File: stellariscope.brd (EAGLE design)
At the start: 60.5 x 60.5 mm, 29 parts, among them U1 74238, U2 74238, U3 TLC5947PWP, U4 TLC59213, U5 741G79DCT, U6 74AHC1G126DBV, U7 74AHC1G126DBV, U8 74AHC1G32DBV, U9 74AHC1G32DBV

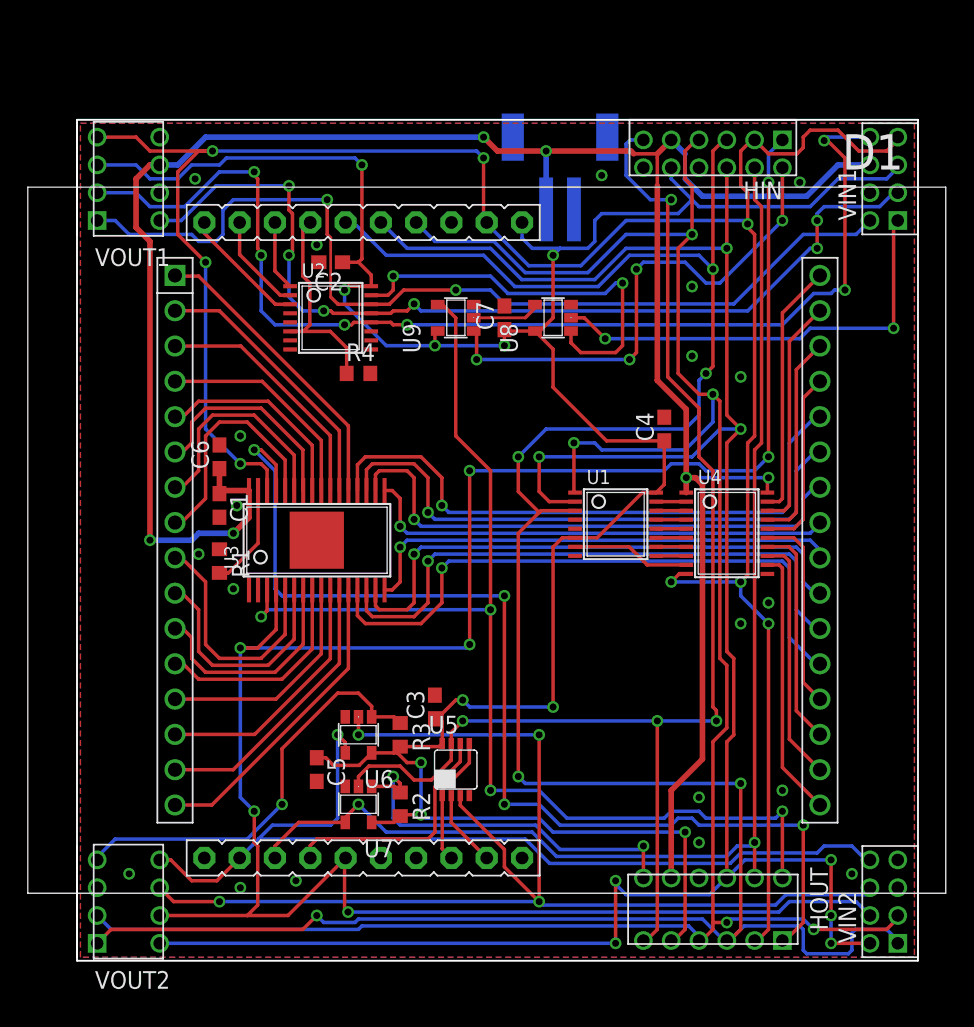
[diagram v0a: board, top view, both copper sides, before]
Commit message: This update fixes the issues with the board counting logic in the first edition. It also adds a driver to the XLAT line in order to prevent fanout problems in large array. This version has not been built and is unlikely to be built.
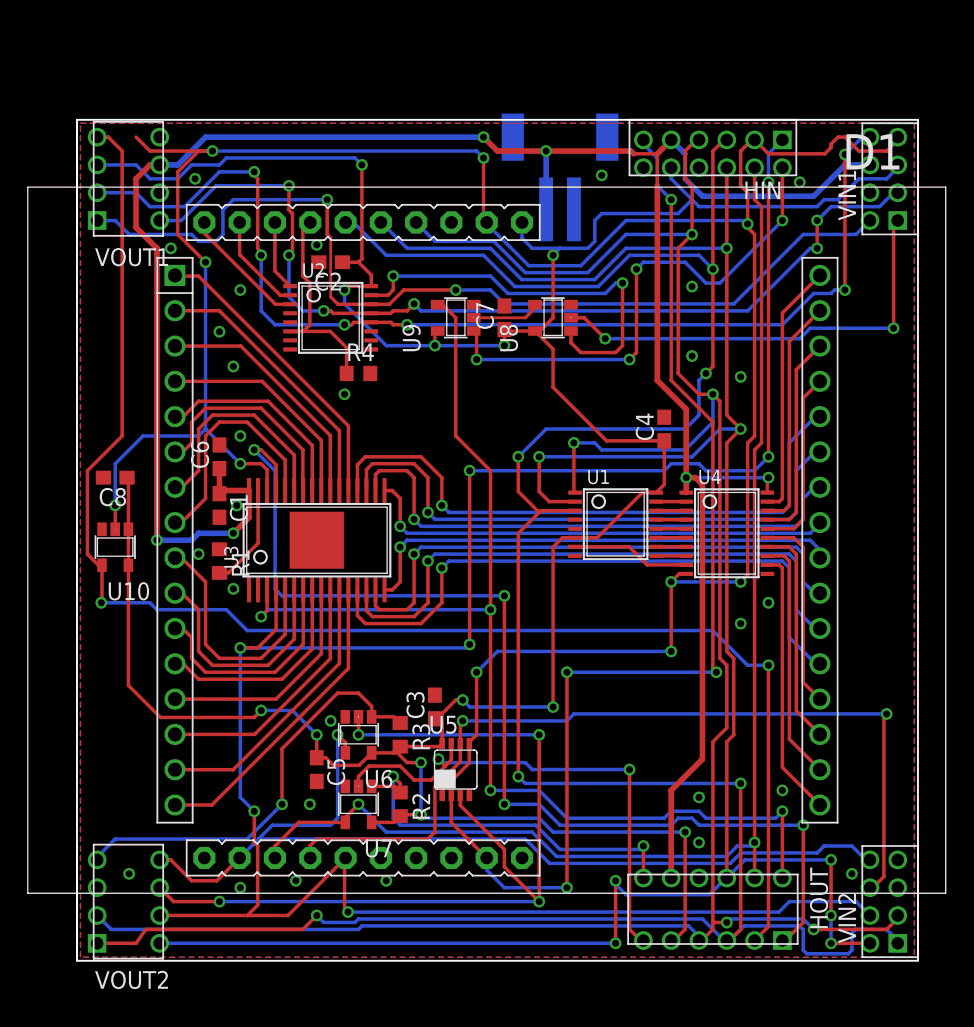
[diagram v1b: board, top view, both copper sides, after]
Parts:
- added C8: 100n, resistor:C0603
- added U10: 74AHC1G126DBV, 74xx-little-us:SOT23-5
- C1, C2, C3, C4, C5, C7: value (none) -> 100n
- C6: value (none) -> 1u
- R1: value (none) -> 2K7
- R2, R3, R4: value (none) -> 10K
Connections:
- net +3V3: now also C8.1, U10.1, U10.5
- net GND: now also C8.2, U10.3
- net HCNT_OUT: no longer HIN.11
- net N$28: now also HOUT.3, U10.4, VOUT1.7; no longer LAUNCHPAD.P2.7, U5.1, U5.5
- net N$37: now also HIN.11
- net N$38: now also VIN2.6
- net VCNT_OUT: no longer VIN2.6
- net XLAT: now also U10.2, U5.1, U5.5; no longer HOUT.3, VOUT1.7
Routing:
- net N$28: track 9.32 -> 106.4 mm, vias 0 -> 2
- net N$37: track 5.54 -> 79.4 mm, vias 0 -> 4
- net HCNT_OUT: track 93.1 -> 37.5 mm, vias 4 -> 2
- net N$38: track 17.4 -> 62.9 mm, vias 0 -> 2
- net +3V3: track 190.7 -> 222.7 mm, vias 10 -> 12
- net VCNT_OUT: track 88.5 -> 64.0 mm
- net XLAT: track 164.0 -> 175.1 mm, vias 8 -> 10
- net N$27: track 81.4 -> 78.9 mm

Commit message: -- Rotated Launchpad footprint to align with LED array -- Swapped vertical connectors to improve routing post-rotation -- Switched power on TLC5947 to 3V3, in order to accomodate logic levels -- Relocated power and horizontal connectors to midline (more or less) -- Added mounting holes
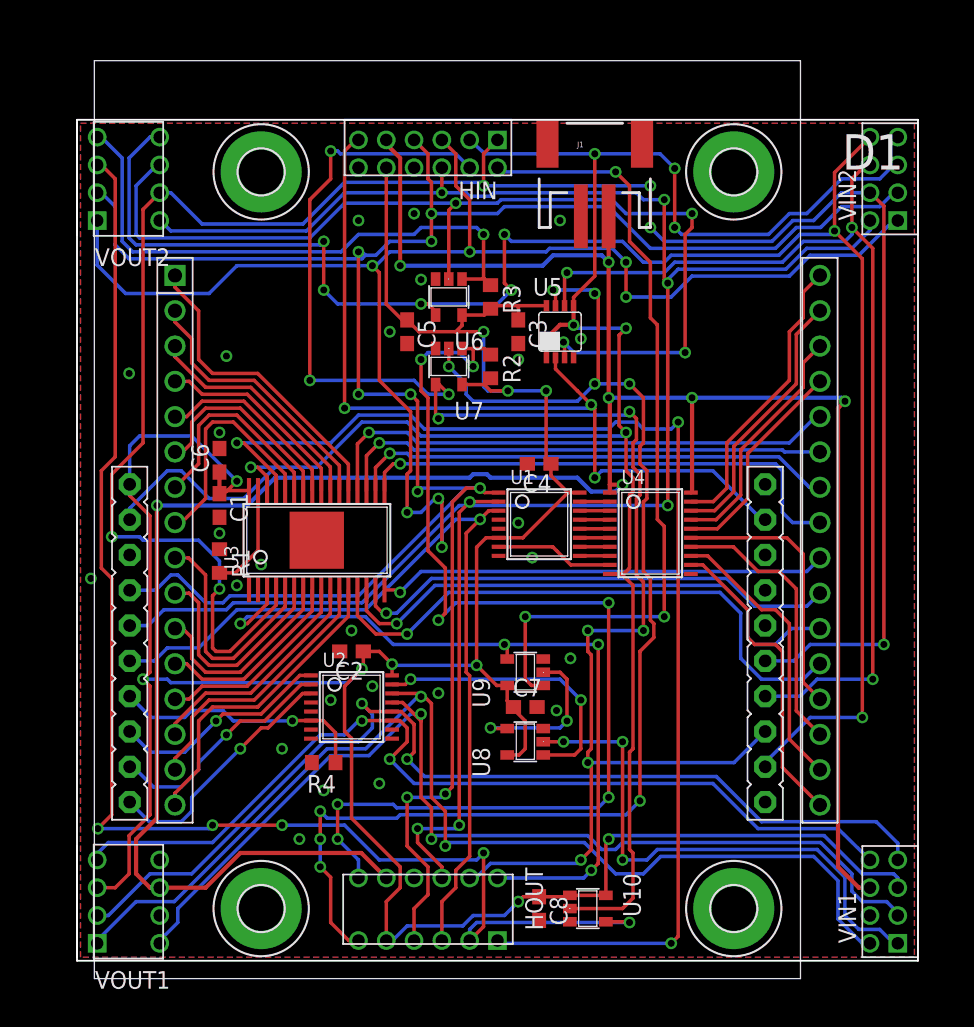
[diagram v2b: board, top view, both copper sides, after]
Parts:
- added H1, H2, H3, H4: MOUNT-PAD-ROUND3.2, holes:3,2-PAD
- moved LAUNCHPAD 61.9 mm to (1.00, 64.5), turned to 270 degrees
- moved VIN1 52.0 mm to (57.8, 4.00)
- moved VIN2 52.0 mm to (57.8, 56.0)
- moved VOUT1 52.0 mm to (3.45, 4.00)
- moved VOUT2 52.0 mm to (3.45, 56.0)
- moved C8 43.5 mm to (33.0, 3.50), turned to 270 degrees
- moved U10 42.8 mm to (36.5, 3.50), turned to 270 degrees
- moved U5 32.4 mm to (34.5, 45.0)
- moved C5 32.2 mm to (23.5, 45.0)
- moved R2 32.2 mm to (29.5, 42.5)
- moved R3 32.2 mm to (29.5, 47.5)
- moved U6 32.2 mm to (26.5, 47.5)
- moved U7 32.2 mm to (26.5, 42.5)
- moved U8 30.6 mm to (32.0, 15.5)
- moved R4 28.1 mm to (17.5, 14.0), turned to 180 degrees
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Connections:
- removed net N$28: HOUT.3, U10.4, VOUT1.7
- new net N$41: U2.11, VIN1.8, VOUT1.7
- new net XLAT_OUT: HOUT.3, U10.4, VOUT2.5
- net +3V3: now also C1.1, C6.1, U3.32
- net +5V: no longer C1.1, C6.1, U3.32
- net GND: now also H1.B3,2, H2.B3,2, H3.B3,2, H4.B3,2
- net N$27: now also VIN1.7; no longer VIN1.8
- net XLAT: now also VIN2.5; no longer VIN1.7
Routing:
- net N$28: track 106.4 -> 0.00 mm, vias 2 -> 0
- net XLAT_OUT: track 0.00 -> 99.6 mm, vias 0 -> 5
- net N$41: track 0.00 -> 67.2 mm, vias 0 -> 2
- net HCNT_OUT: track 37.5 -> 93.4 mm, vias 2 -> 9
- net VCNT_IN: track 68.5 -> 124.2 mm, vias 1 -> 7
- net HSENSE: track 27.9 -> 80.2 mm, vias 2 -> 7
- net N$48: track 82.8 -> 54.9 mm
- net HCNT_IN: track 90.3 -> 115.7 mm, vias 2 -> 9
- net +5V: track 165.6 -> 188.9 mm, vias 6 -> 7
- net XLAT: track 175.1 -> 153.4 mm, vias 10 -> 7
- net N$25: track 36.8 -> 58.1 mm, vias 4 -> 3
- net N$37: track 79.4 -> 61.4 mm, vias 4 -> 3
- net N$34: track 183.2 -> 166.0 mm, vias 6 -> 8
- net N$39: track 68.9 -> 81.5 mm
- net SOUT: track 77.8 -> 88.8 mm, vias 4 -> 3
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
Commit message: -- Moved the old demo code to led test -- First commit of new demo code -- Updated hardware design 	-- Add 10 uF decoupling caps for board & anode drive 	-- tied latch and blank lines together
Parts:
- removed H4: MOUNT-PAD-ROUND3.2, holes:3,2-PAD
- removed J1: (no value), SparkFun-Connectors:JST-2-SMD
- added JP1: (no value), pinhead:1X03
- added JP2: (no value), pinhead-1:1X02/90
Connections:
- net +5V: now also JP1.3, JP2.1; no longer J1.2
- net GND: now also JP1.1, JP1.2, JP2.2; no longer H4.B3,2, J1.1, U3.2
- net XLAT: now also U3.2
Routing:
- net +5V: track 188.9 -> 200.8 mm, vias 7 -> 8
- net XLAT: track 153.4 -> 157.3 mm
- net SIN: track 152.2 -> 155.4 mm
- net N$25: track 58.1 -> 61.1 mm
- net N$35: track 154.9 -> 156.2 mm
- net VCNT_OUT: track 73.6 -> 74.4 mm

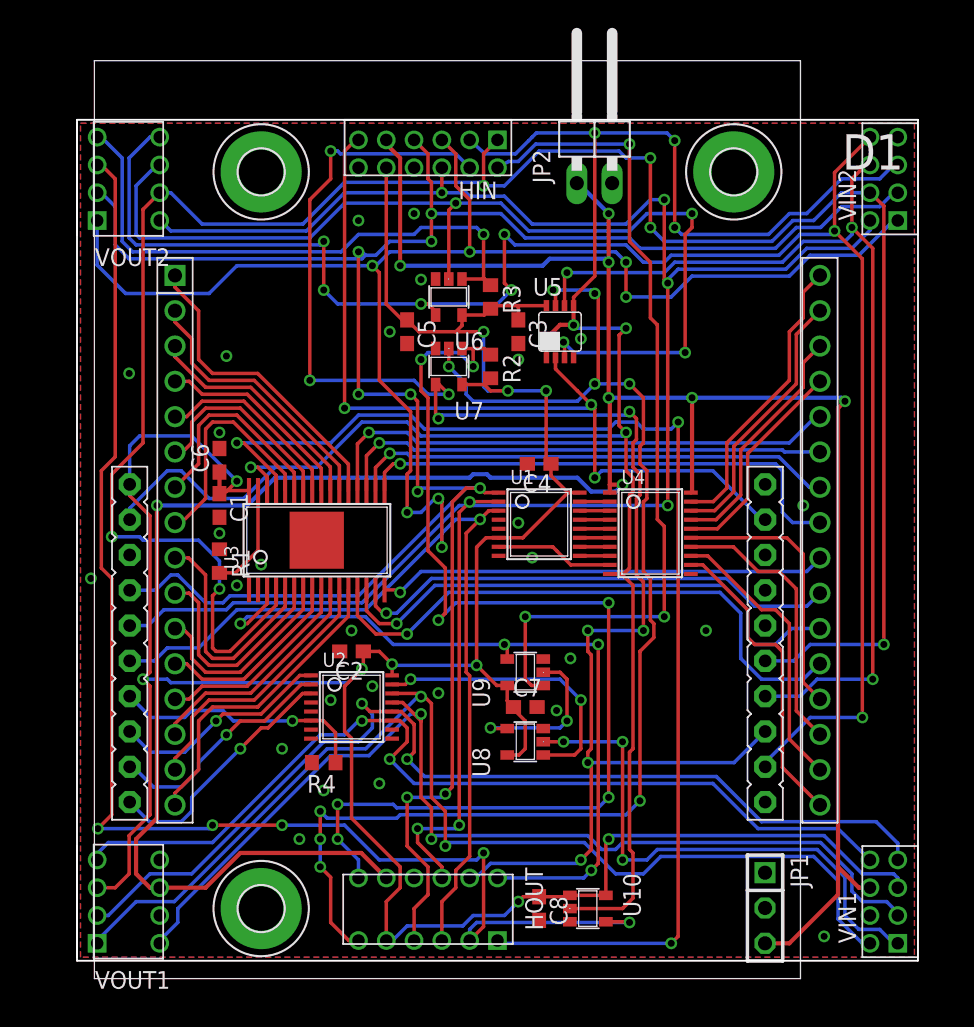
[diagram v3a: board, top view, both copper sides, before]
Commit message: -- Modified pinout to allow UART to function correctly
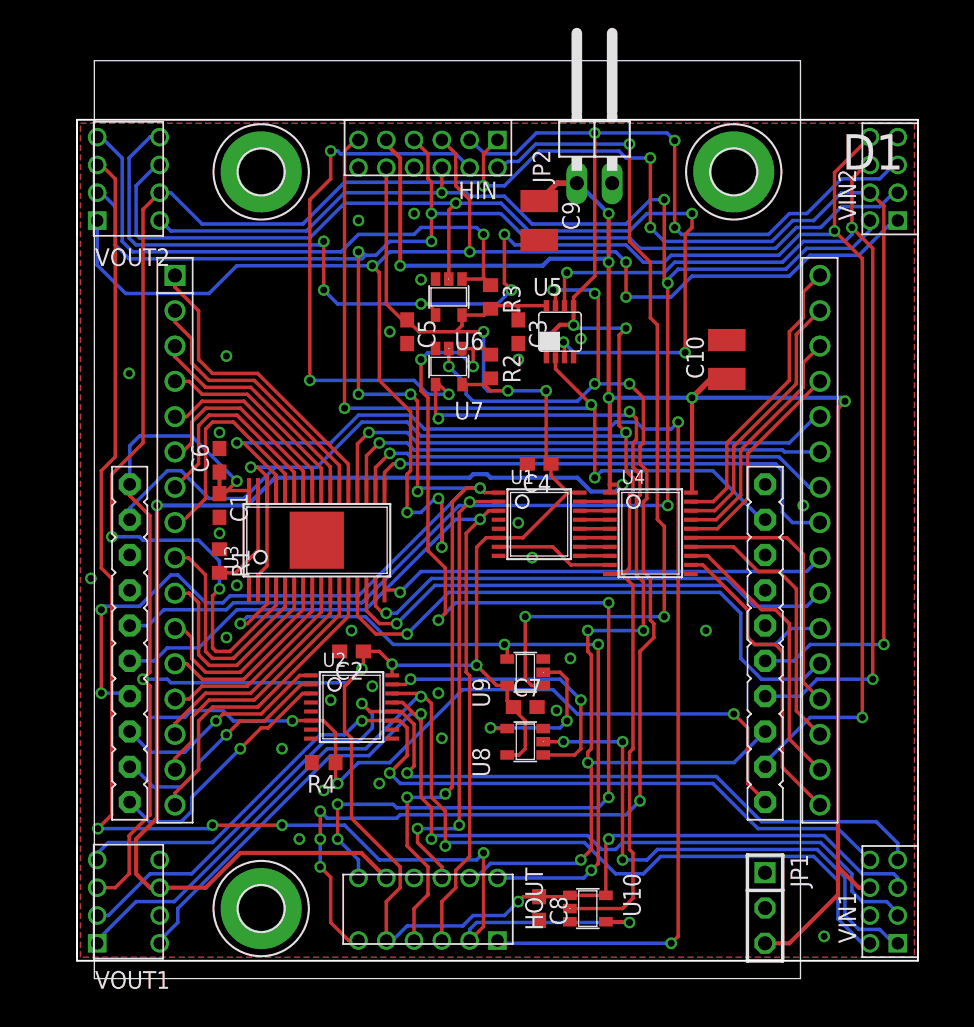
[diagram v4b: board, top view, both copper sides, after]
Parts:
- added C10, C9: 10u, resistor:C1210
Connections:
- net +5V: now also C10.1, C9.1
- net GND: now also C10.2, C9.2
- net N$29: now also LAUNCHPAD.P2.3; no longer LAUNCHPAD.P1.5
- net N$36: now also LAUNCHPAD.P1.5; no longer LAUNCHPAD.P1.2
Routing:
- net N$29: track 18.5 -> 57.2 mm, vias 1 -> 3
- net N$36: track 168.2 -> 178.9 mm, vias 9 -> 11
- net XLAT: track 157.3 -> 164.7 mm
- net +5V: track 200.8 -> 207.2 mm
- net N$27: track 73.5 -> 74.1 mm
- net N$41: track 67.2 -> 67.8 mm
